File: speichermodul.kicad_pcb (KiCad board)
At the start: 2 copper layers, 100 x 160 mm, 14 parts, among them P7 CONN_01X01, P8 CONN_02X10, P9 CONN_02X10, U5 74LS540, U6 74LS540

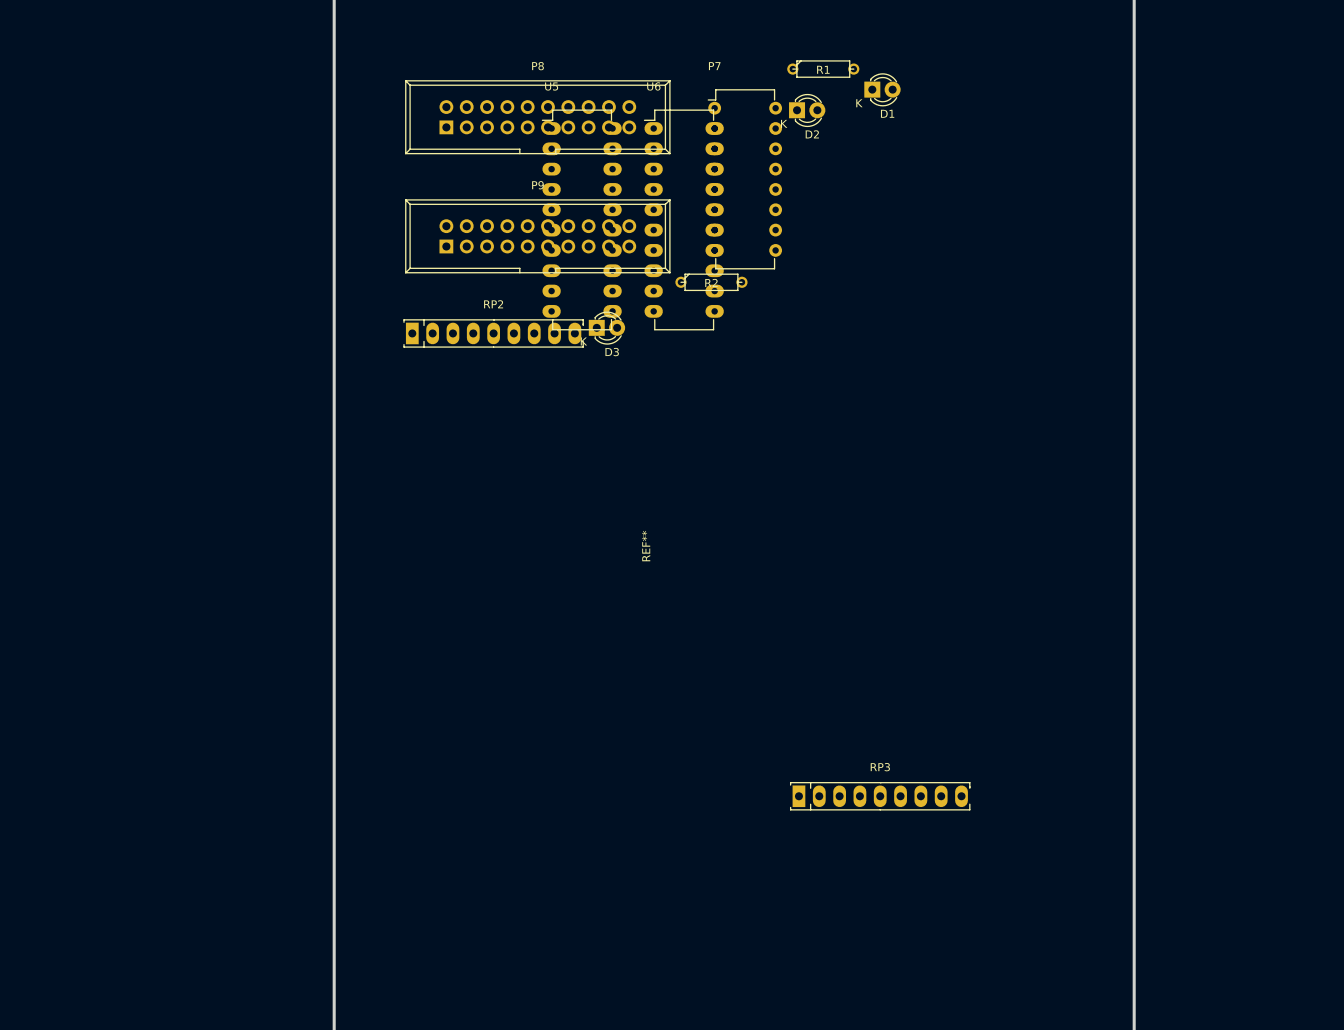
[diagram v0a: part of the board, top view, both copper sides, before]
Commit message: einige DIPs hinzugefügt
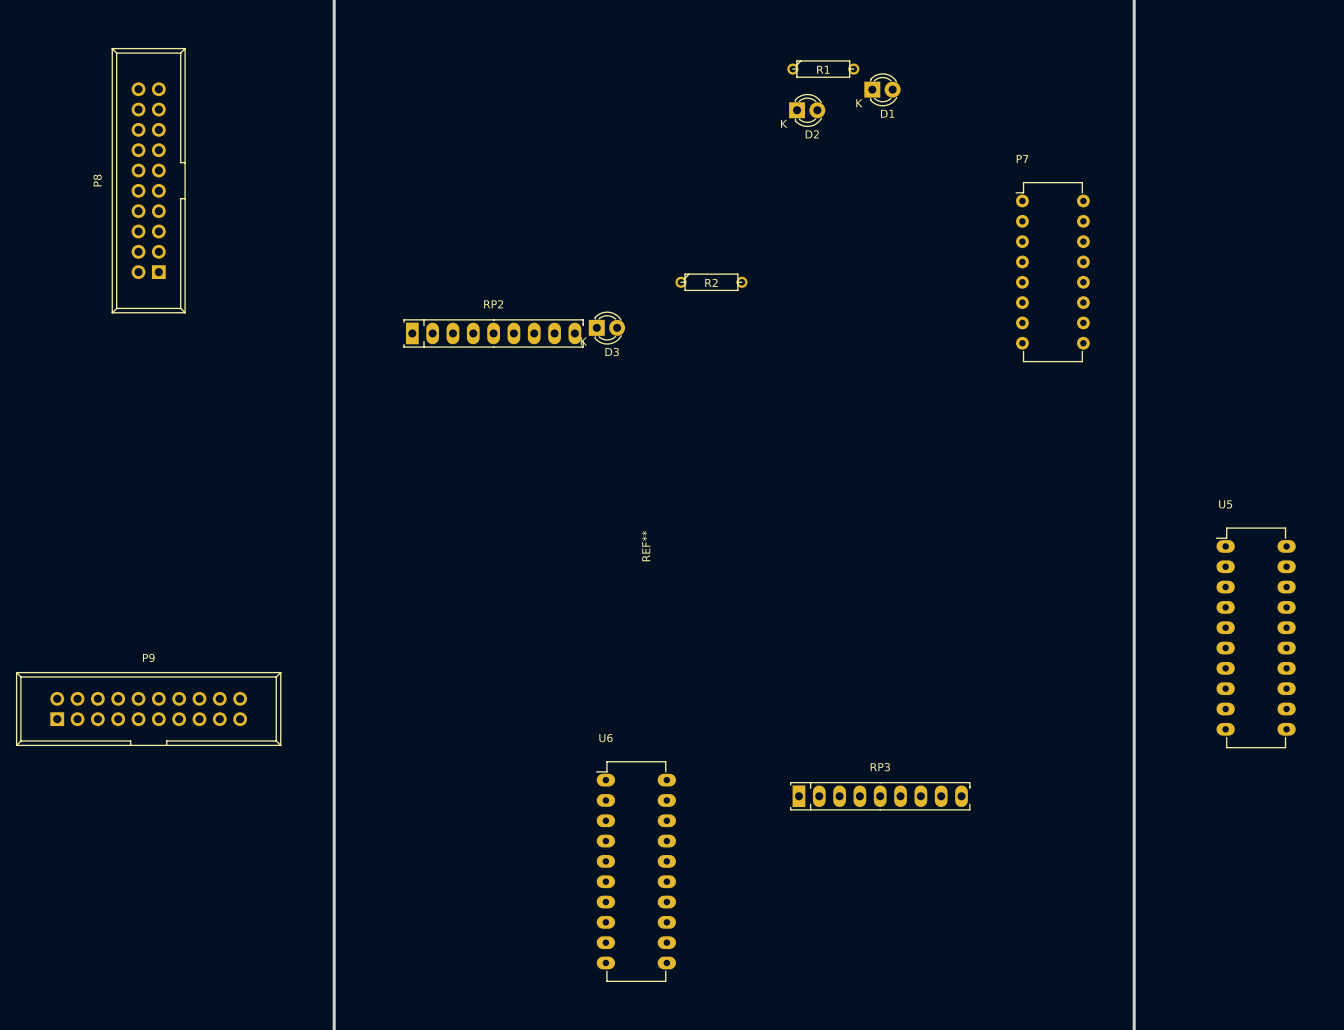
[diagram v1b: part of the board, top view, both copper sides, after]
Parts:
- moved U5 99.1 mm to (139.7, 109.2)
- moved U6 81.7 mm to (62.2, 138.4)
- moved P9 76.5 mm to (-6.35, 130.8)
- moved P8 40.2 mm to (6.35, 74.9), turned to 90 degrees
- moved P7 40.2 mm to (114.3, 66.0)

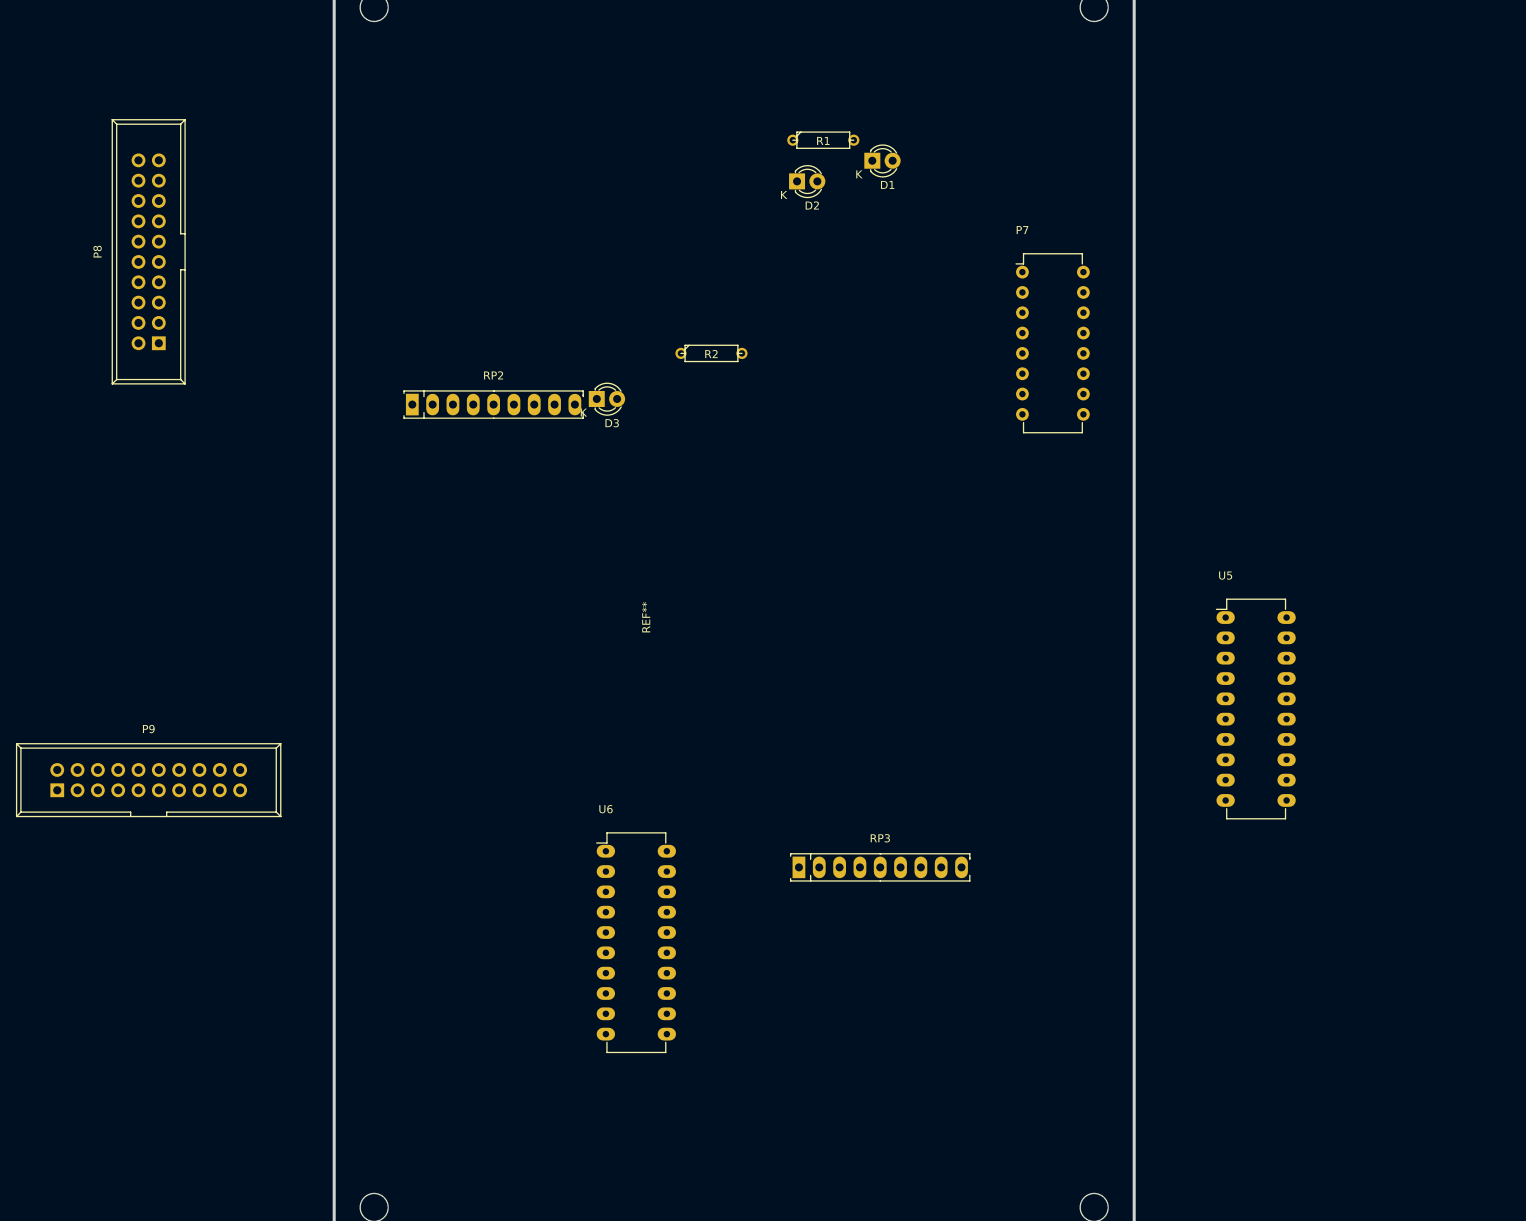
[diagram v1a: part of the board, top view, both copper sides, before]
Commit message: Bauteile hinzugefügt
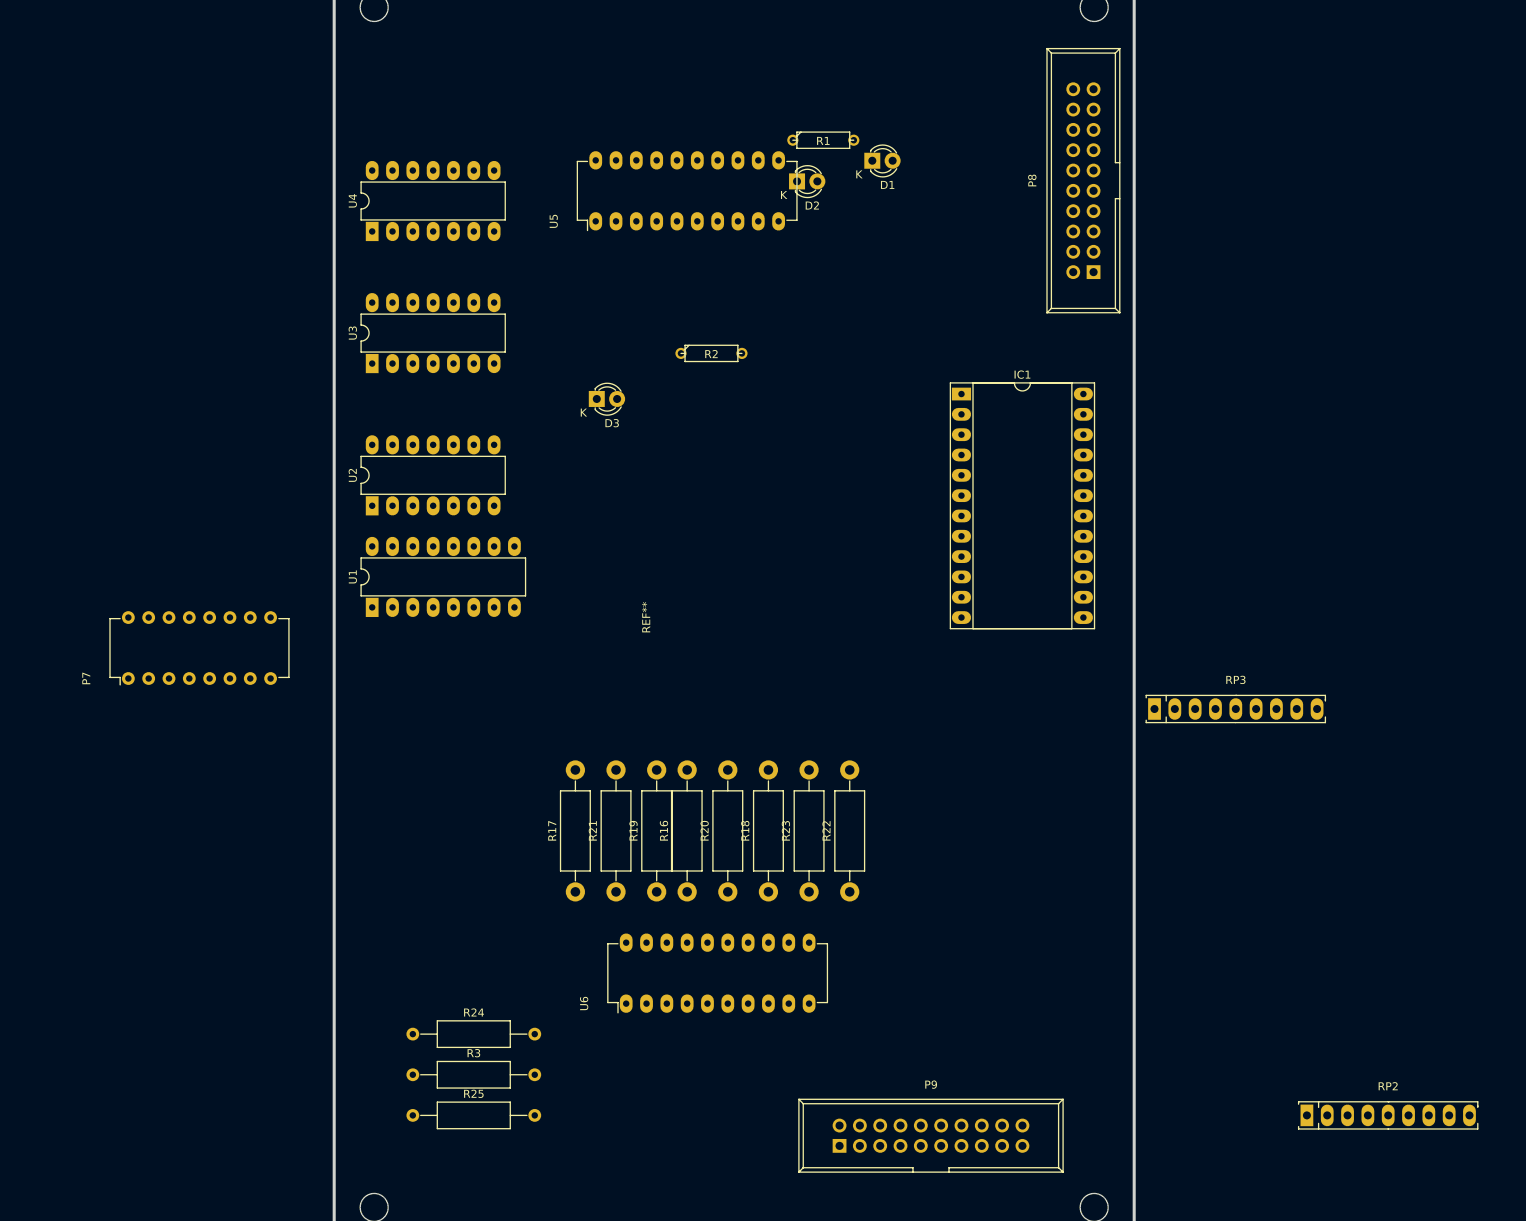
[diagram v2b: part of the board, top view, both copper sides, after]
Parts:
- added IC1: 6116, Housings_DIP:DIP-24_W15.24mm_Socket_LongPads, F.Cu at (106.7, 81.3)
- added R16: 330, Resistors_ThroughHole:R_Axial_DIN0411_L9.9mm_D3.6mm_P15.24mm_Horizontal, F.Cu at (72.4, 143.5)
- added R17: 330, Resistors_ThroughHole:R_Axial_DIN0411_L9.9mm_D3.6mm_P15.24mm_Horizontal, F.Cu at (58.4, 143.5)
- added R18: 330, Resistors_ThroughHole:R_Axial_DIN0411_L9.9mm_D3.6mm_P15.24mm_Horizontal, F.Cu at (82.5, 143.5)
- added R19: 330, Resistors_ThroughHole:R_Axial_DIN0411_L9.9mm_D3.6mm_P15.24mm_Horizontal, F.Cu at (68.6, 143.5)
- added R20: 330, Resistors_ThroughHole:R_Axial_DIN0411_L9.9mm_D3.6mm_P15.24mm_Horizontal, F.Cu at (77.5, 143.5)
- added R21: 330, Resistors_ThroughHole:R_Axial_DIN0411_L9.9mm_D3.6mm_P15.24mm_Horizontal, F.Cu at (63.5, 143.5)
- added R22: 330, Resistors_ThroughHole:R_Axial_DIN0411_L9.9mm_D3.6mm_P15.24mm_Horizontal, F.Cu at (92.7, 143.5)
- added R23: 330, Resistors_ThroughHole:R_Axial_DIN0411_L9.9mm_D3.6mm_P15.24mm_Horizontal, F.Cu at (87.6, 143.5)
- added R24: 4,7k, Resistors_ThroughHole:R_Axial_DIN0309_L9.0mm_D3.2mm_P15.24mm_Horizontal, F.Cu at (38.1, 161.3)
- added R25: 4,7k, Resistors_ThroughHole:R_Axial_DIN0309_L9.0mm_D3.2mm_P15.24mm_Horizontal, F.Cu at (38.1, 171.4)
- added R3: 4,7k, Resistors_ThroughHole:R_Axial_DIN0309_L9.0mm_D3.2mm_P15.24mm_Horizontal, F.Cu at (38.1, 166.4)
- added U1: 7400, Housings_DIP:DIP-16_W7.62mm_LongPads, F.Cu at (33.0, 108.0)
- added U2: 74LS08, Housings_DIP:DIP-14_W7.62mm_LongPads, F.Cu at (33.0, 95.2)
- added U3: 74LS08, Housings_DIP:DIP-14_W7.62mm_LongPads, F.Cu at (33.0, 77.5)
- added U4: 74LS14, Housings_DIP:DIP-14_W7.62mm_LongPads, F.Cu at (33.0, 61.0)
- moved RP2 142.8 mm to (160.0, 171.4)
- moved P7 122.8 mm to (2.54, 116.8), turned to 90 degrees
- moved P8 117.2 mm to (123.2, 66.0)
- moved P9 107.4 mm to (91.4, 175.3)
- moved U5 93.0 mm to (61.0, 59.7), turned to 90 degrees
- moved RP3 48.7 mm to (141.0, 120.7)
- moved U6 19.2 mm to (64.8, 157.5), turned to 90 degrees

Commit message: einige Leds und Resistoren hinzugefügt und ausgebessert
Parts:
- added D10: LED, LEDs:LED_D1.8mm_W1.8mm_H2.4mm_Horizontal_O3.81mm_Z8.2mm, F.Cu at (85.1, 30.5)
- added D11: LED, LEDs:LED_D1.8mm_W1.8mm_H2.4mm_Horizontal_O3.81mm_Z8.2mm, F.Cu at (54.6, 118.1)
- added D12: LED, LEDs:LED_D1.8mm_W1.8mm_H2.4mm_Horizontal_O3.81mm_Z8.2mm, F.Cu at (69.8, 118.1)
- added D13: LED, LEDs:LED_D1.8mm_W1.8mm_H2.4mm_Horizontal_O3.81mm_Z8.2mm, F.Cu at (74.9, 118.1)
- added D14: LED, LEDs:LED_D1.8mm_W1.8mm_H2.4mm_Horizontal_O3.81mm_Z8.2mm, F.Cu at (78.7, 118.1)
- added D15: LED, LEDs:LED_D1.8mm_W1.8mm_H2.4mm_Horizontal_O3.81mm_Z8.2mm, F.Cu at (83.8, 118.1)
- added D16: LED, LEDs:LED_D1.8mm_W1.8mm_H2.4mm_Horizontal_O3.81mm_Z8.2mm, F.Cu at (88.9, 118.1)
- added D17: LED, LEDs:LED_D1.8mm_W1.8mm_H2.4mm_Horizontal_O3.81mm_Z8.2mm, F.Cu at (64.8, 118.1)
- added D18: LED, LEDs:LED_D1.8mm_W1.8mm_H2.4mm_Horizontal_O3.81mm_Z8.2mm, F.Cu at (59.7, 118.1)
- added D4: LED, LEDs:LED_D1.8mm_W1.8mm_H2.4mm_Horizontal_O3.81mm_Z8.2mm, F.Cu at (55.9, 30.5)
- added D5: LED, LEDs:LED_D1.8mm_W1.8mm_H2.4mm_Horizontal_O3.81mm_Z8.2mm, F.Cu at (59.7, 30.5)
- added D6: LED, LEDs:LED_D1.8mm_W1.8mm_H2.4mm_Horizontal_O3.81mm_Z8.2mm, F.Cu at (64.8, 30.5)
- added D7: LED, LEDs:LED_D1.8mm_W1.8mm_H2.4mm_Horizontal_O3.81mm_Z8.2mm, F.Cu at (69.8, 30.5)
- added D8: LED, LEDs:LED_D1.8mm_W1.8mm_H2.4mm_Horizontal_O3.81mm_Z8.2mm, F.Cu at (74.9, 30.5)
- added D9: LED, LEDs:LED_D1.8mm_W1.8mm_H2.4mm_Horizontal_O3.81mm_Z8.2mm, F.Cu at (80.0, 30.5)
- added R10: 330, Resistors_ThroughHole:R_Axial_DIN0411_L9.9mm_D3.6mm_P15.24mm_Horizontal, F.Cu at (91.4, 55.9)
- added R11: 330, Resistors_ThroughHole:R_Axial_DIN0411_L9.9mm_D3.6mm_P15.24mm_Horizontal, F.Cu at (71.1, 55.9)
- added R12: 330, Resistors_ThroughHole:R_Axial_DIN0411_L9.9mm_D3.6mm_P15.24mm_Horizontal, F.Cu at (76.2, 55.9)
- added R13: 330, Resistors_ThroughHole:R_Axial_DIN0411_L9.9mm_D3.6mm_P15.24mm_Horizontal, F.Cu at (66.0, 55.9)
- added R14: 330, Resistors_ThroughHole:R_Axial_DIN0411_L9.9mm_D3.6mm_P15.24mm_Horizontal, F.Cu at (81.3, 55.9)
- added R15: 330, Resistors_ThroughHole:R_Axial_DIN0411_L9.9mm_D3.6mm_P15.24mm_Horizontal, F.Cu at (96.5, 55.9)
- added R4: 330, Resistors_ThroughHole:R_Axial_DIN0411_L9.9mm_D3.6mm_P15.24mm_Horizontal, F.Cu at (59.7, 55.9)
- added R9: 330, Resistors_ThroughHole:R_Axial_DIN0411_L9.9mm_D3.6mm_P15.24mm_Horizontal, F.Cu at (86.4, 55.9)
- D3: footprint LEDs:LED-3MM -> LEDs:LED_D1.8mm_W1.8mm_H2.4mm_Horizontal_O3.81mm_Z8.2mm
- U1: footprint Housings_DIP:DIP-16_W7.62mm_LongPads -> Housings_DIP:DIP-14_W7.62mm_LongPads
- moved D1 87.5 mm to (120.7, 135.9)
- moved D2 77.3 mm to (119.4, 124.5)
- moved D3 52.4 mm to (50.8, 30.5)
- moved R1 20.8 mm to (109.2, 55.9)
- moved U5 8.98 mm to (62.2, 68.6)
- moved U1 5.08 mm to (33.0, 113.0)
- moved U6 1.80 mm to (63.5, 156.2)

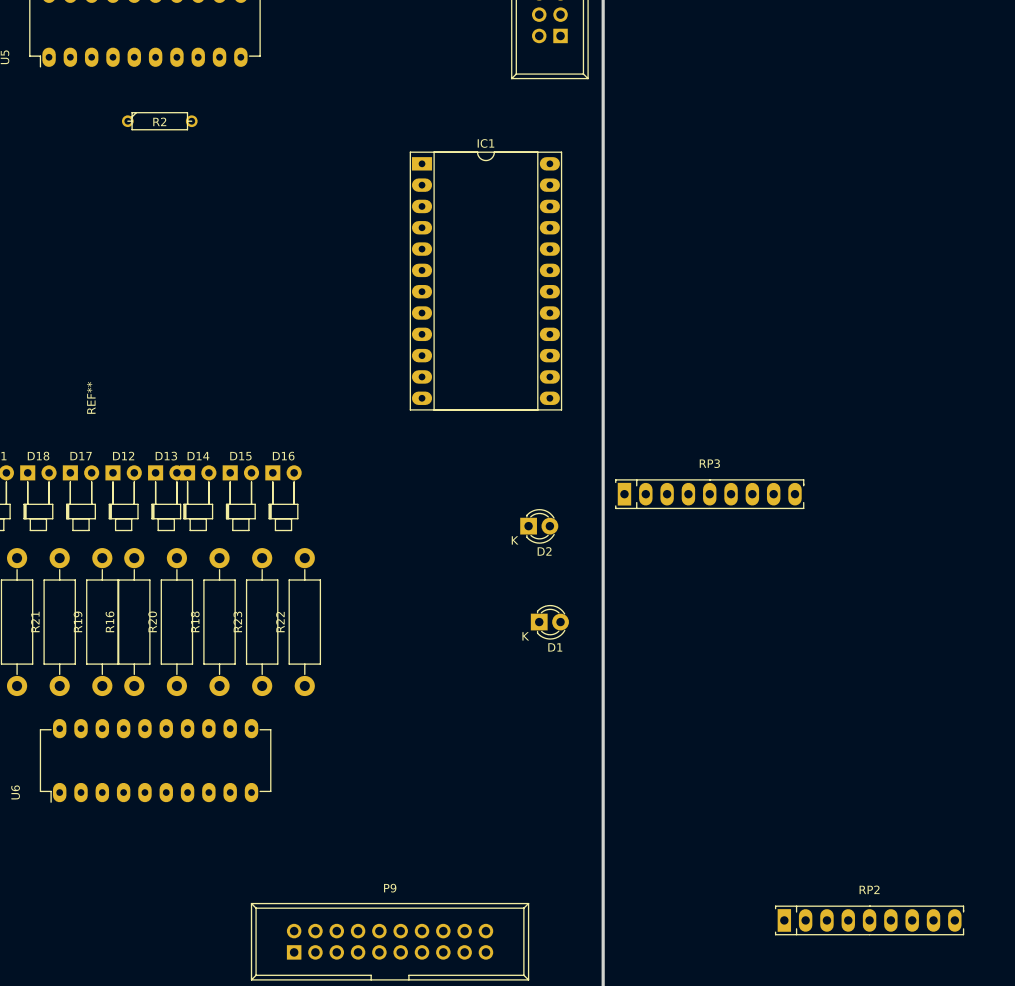
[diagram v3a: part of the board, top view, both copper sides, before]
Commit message: pcb weiter verschobene bauteile
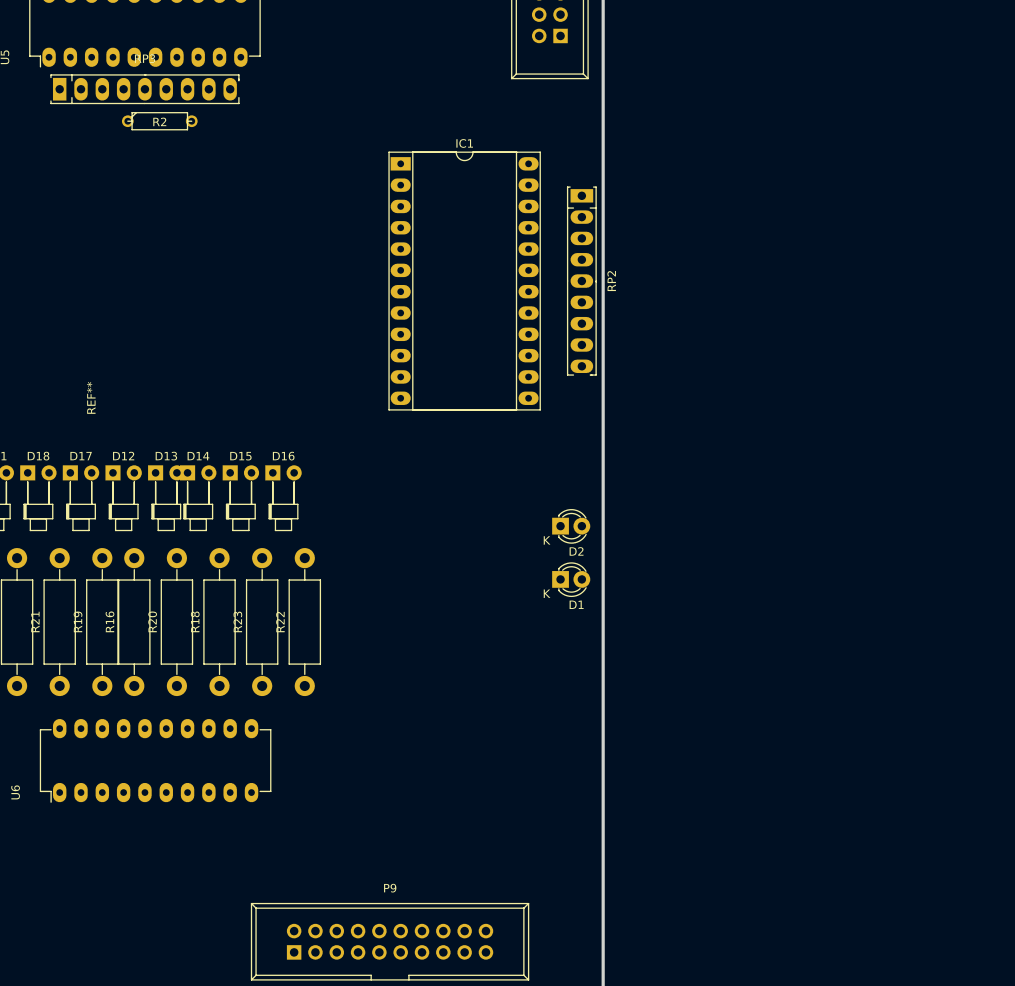
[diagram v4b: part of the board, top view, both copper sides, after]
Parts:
- moved RP2 83.6 mm to (125.7, 95.2), turned to 270 degrees
- moved RP3 82.8 mm to (73.7, 72.4)
- moved D1 5.68 mm to (123.2, 130.8)
- moved D2 3.81 mm to (123.2, 124.5)
- moved IC1 2.54 mm to (104.1, 81.3)
